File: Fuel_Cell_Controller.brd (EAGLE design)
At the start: 203.2 x 163.8 mm, 127 parts, among them J1 BLUETOOTH, U1 MAX232PTH

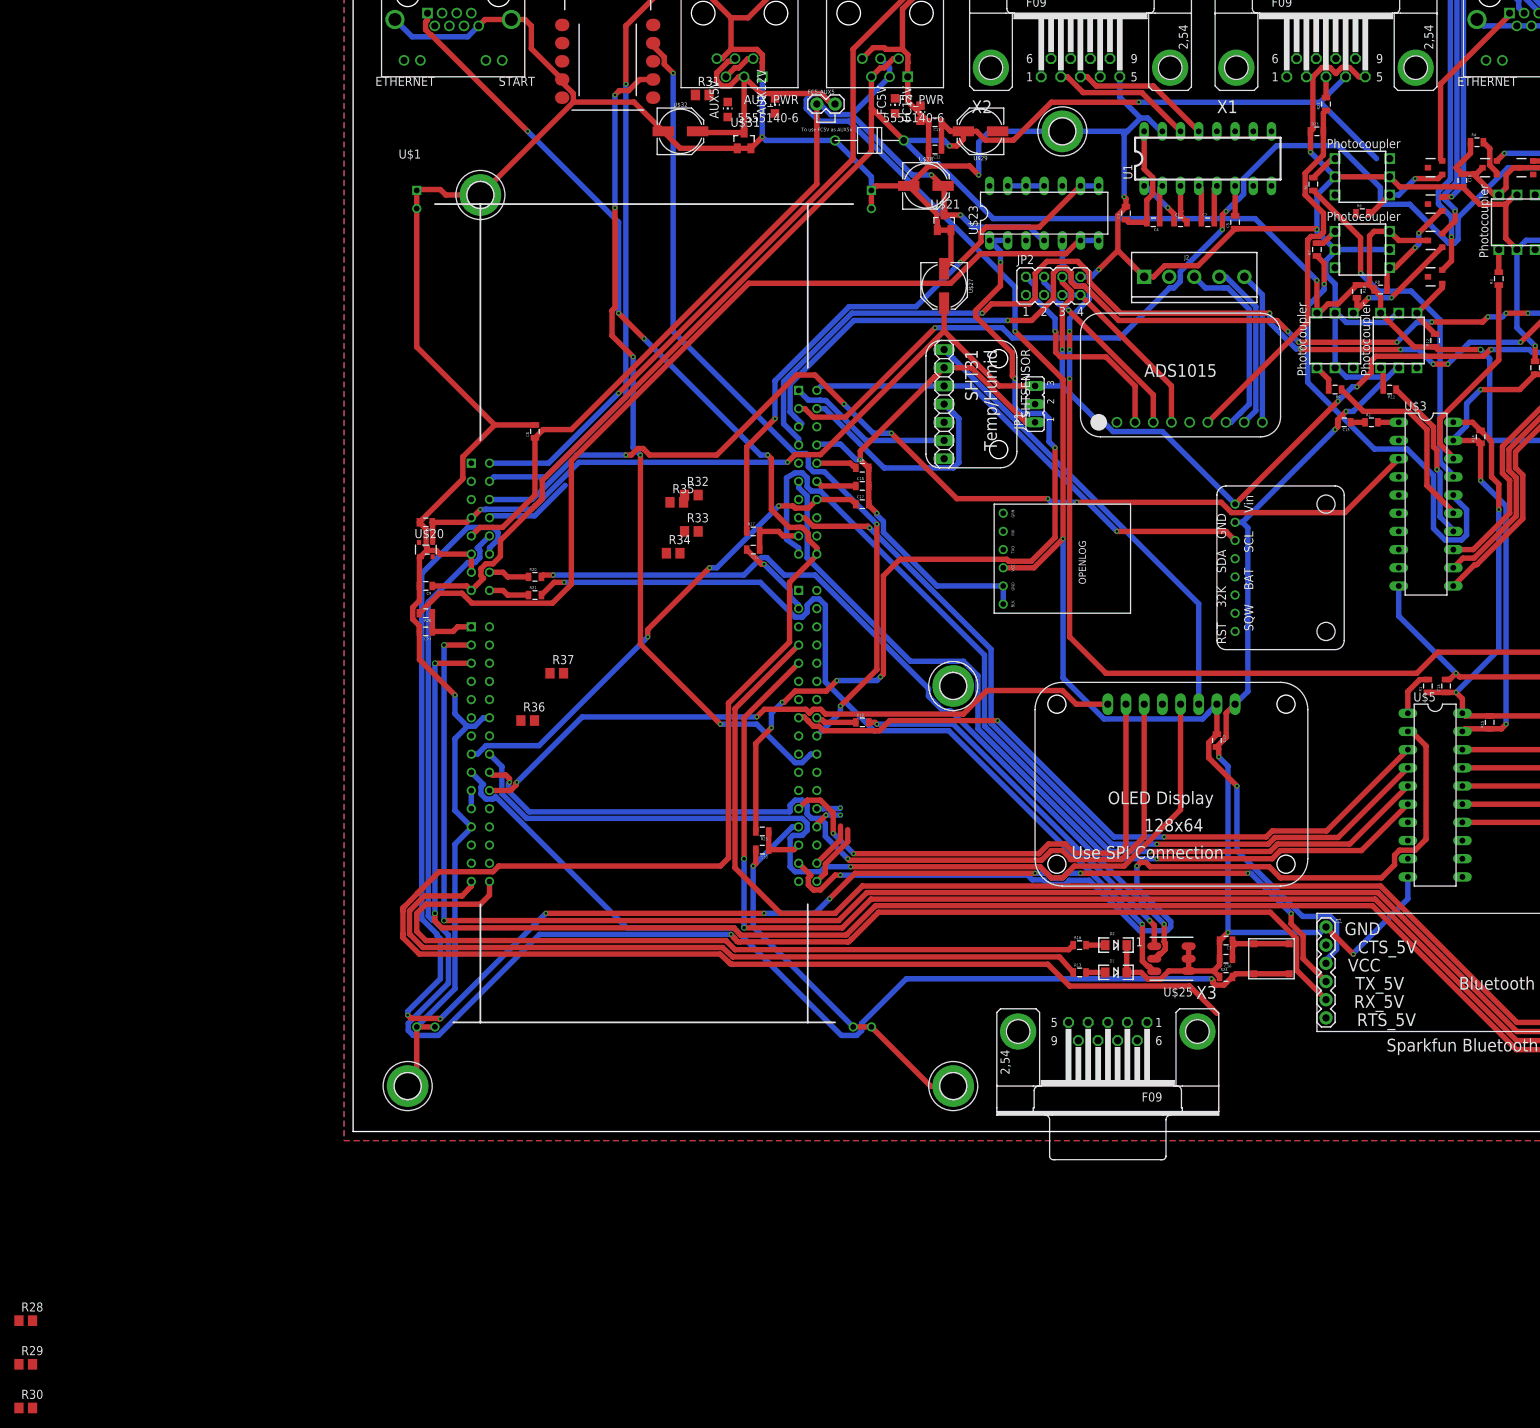
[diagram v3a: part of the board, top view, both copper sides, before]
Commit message: Added some changes in the Schematic to the Board
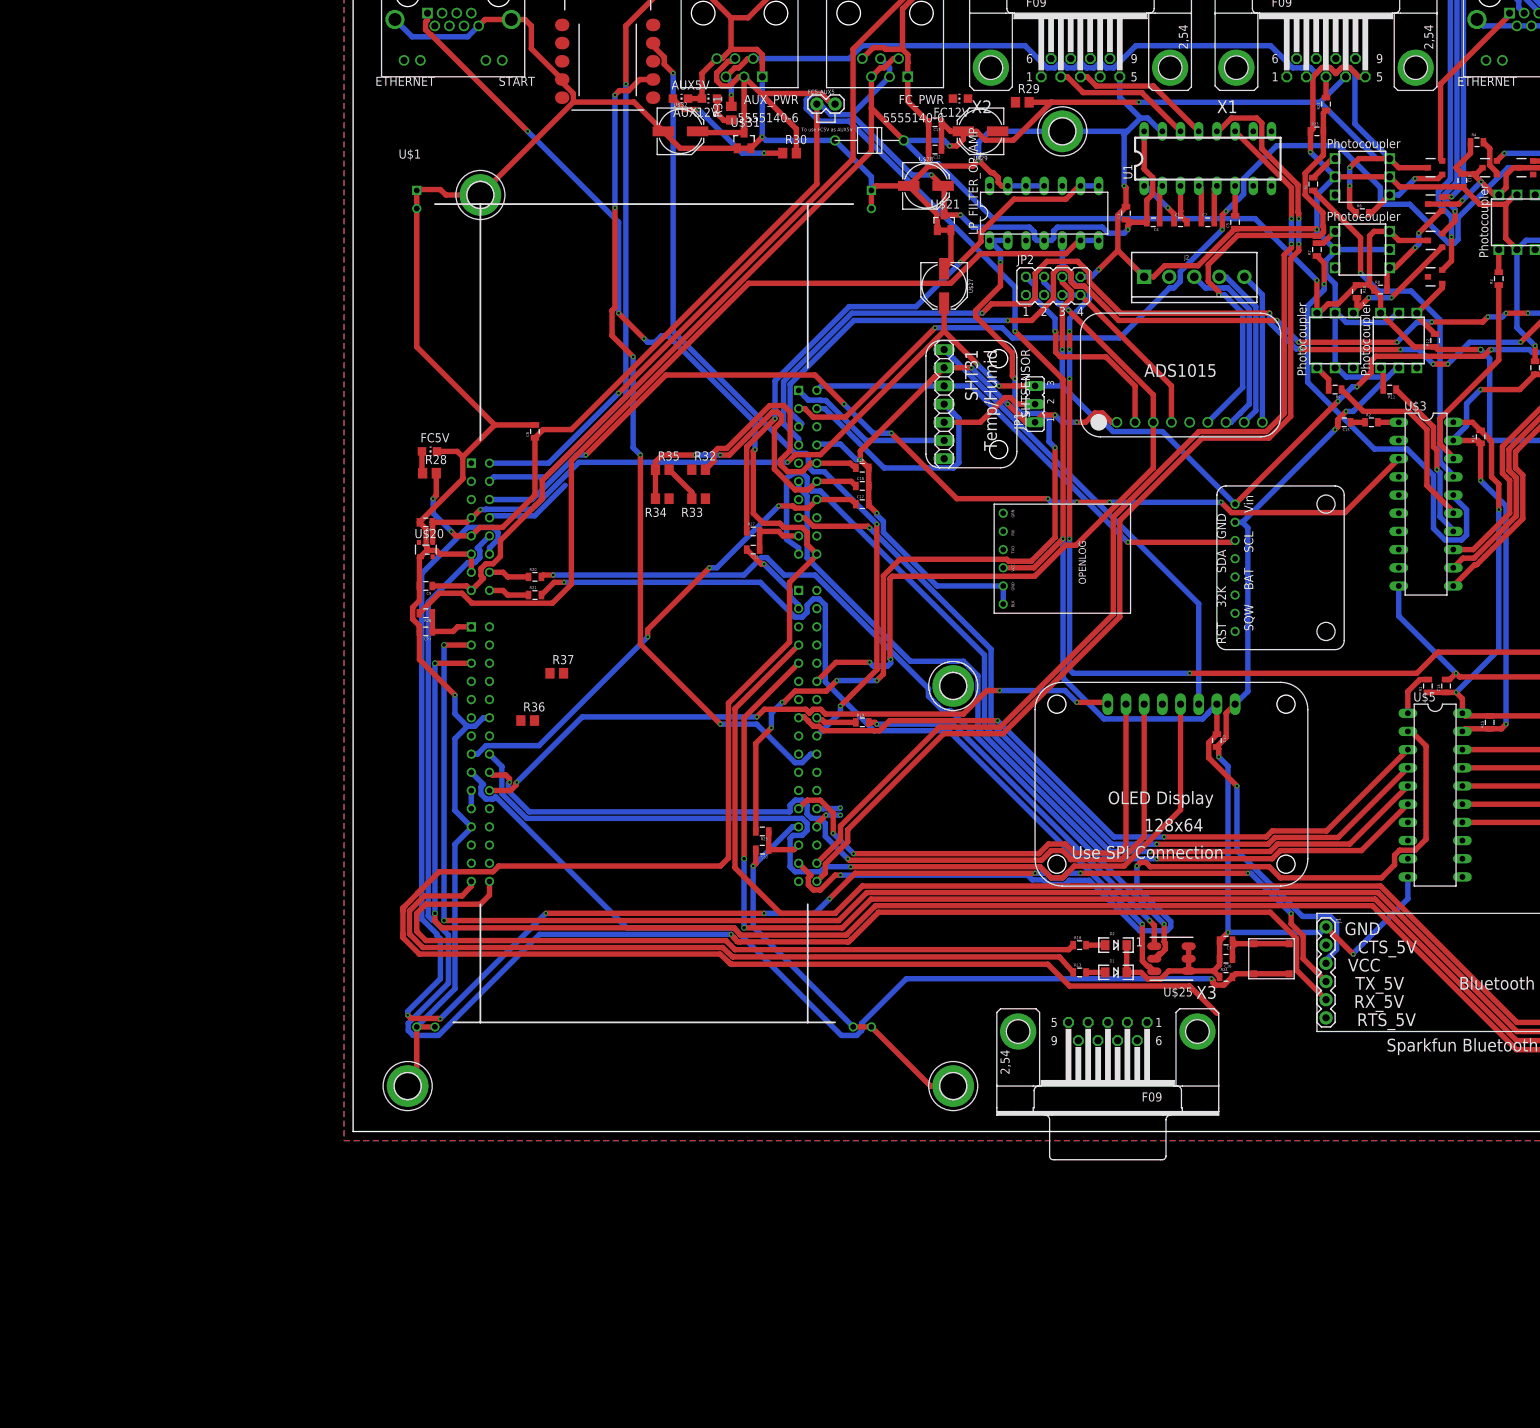
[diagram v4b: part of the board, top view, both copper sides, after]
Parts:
- moved R29 224.6 mm to (93.5, 143.8)
- moved R30 205.2 mm to (61.0, 136.7)
- moved R28 131.1 mm to (10.7, 91.9)
- moved FC5V 81.0 mm to (10.7, 95.0), turned to 270 degrees
- moved AUX12V 9.20 mm to (49.8, 144.3), turned to 90 degrees
- moved R34 7.77 mm to (43.2, 88.4), turned to 180 degrees
- moved AUX5V 6.78 mm to (45.7, 144.3), turned to 270 degrees
- moved FC12V 5.95 mm to (84.8, 144.3), turned to 90 degrees
- moved R35 5.00 mm to (43.2, 92.5)
- moved R31 4.79 mm to (52.8, 142.2), turned to 90 degrees
- moved R33 4.68 mm to (48.3, 88.4), turned to 180 degrees
- moved R32 3.70 mm to (48.3, 92.5)
- renumbered U$23 to LP_FILTER_OP_AMP
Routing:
- net MOTOR_RX: track 9.02 -> 153.6 mm, vias 0 -> 2
- net MOTOR_TX: track 6.57 -> 143.4 mm, vias 0 -> 2
- net AUX12V: track 4.86 -> 134.4 mm, vias 0 -> 3
- net I2C4_SDA: track 26.9 -> 100.1 mm, vias 1 -> 3
- net MOTOR_CURR: track 5.72 -> 47.0 mm, vias 0 -> 2
- net GND: track 1306.4 -> 1341.2 mm, vias 20 -> 24
- net FC_CURR: track 5.72 -> 36.2 mm
- net FC5V: track 265.0 -> 292.7 mm, vias 7 -> 10
- net N$25: track 0.00 -> 18.5 mm, vias 0 -> 2
- net SHT_ADR: track 0.00 -> 14.5 mm
- net FC12V: track 482.1 -> 493.9 mm, vias 5 -> 7
- net MASS_FLOW: track 53.2 -> 63.8 mm, vias 0 -> 1
- net AUX5V: track 222.5 -> 232.9 mm
- net N$28: track 0.00 -> 4.50 mm
- net _START: track 318.7 -> 322.4 mm
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
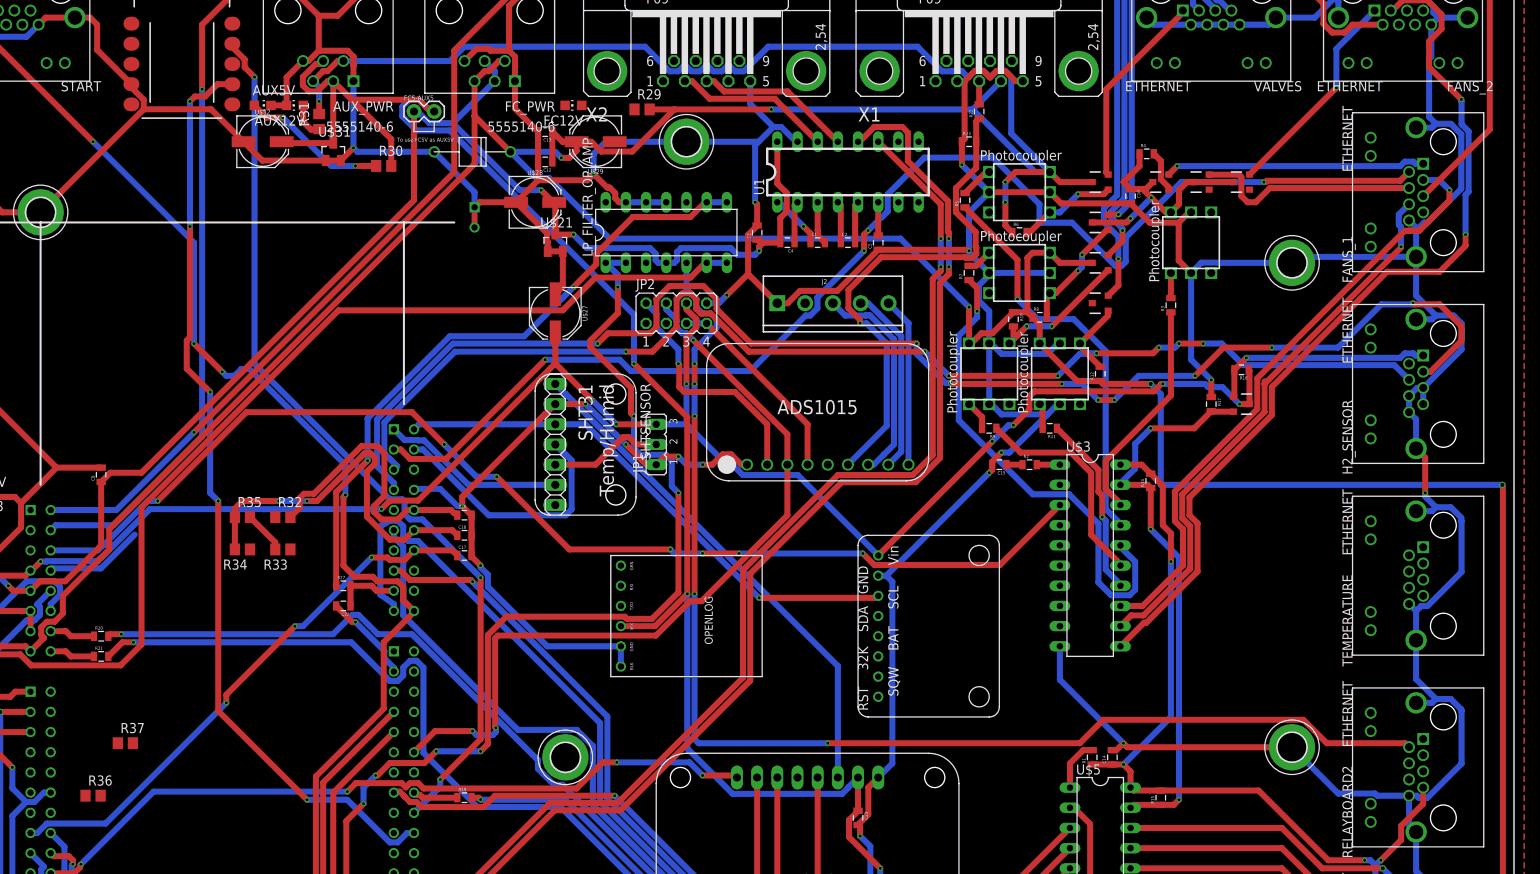
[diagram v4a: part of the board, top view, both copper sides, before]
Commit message: Continued Routing the FCC Board
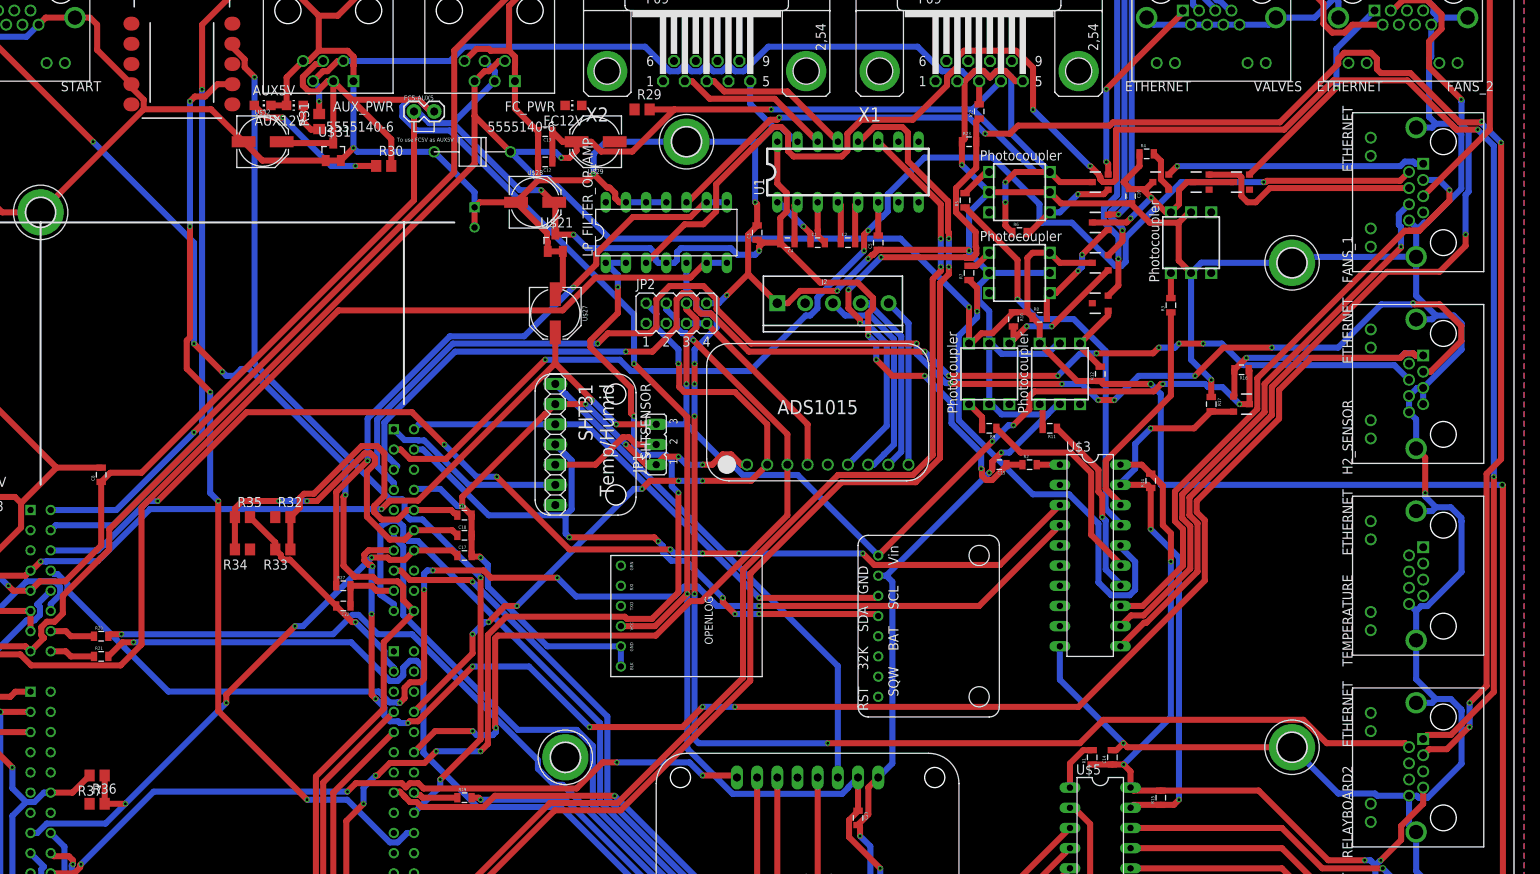
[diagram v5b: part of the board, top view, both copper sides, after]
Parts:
- moved R37 5.40 mm to (24.9, 59.9), turned to 180 degrees
- moved R36 1.14 mm to (24.9, 56.4)
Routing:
- net FC_VOLT: track 0.00 -> 229.3 mm, vias 0 -> 4
- net CAP_VOLT: track 0.00 -> 200.5 mm, vias 0 -> 6
- net STOP: track 28.1 -> 220.1 mm, vias 1 -> 9
- net _PURGE_VALVE: track 12.5 -> 156.9 mm, vias 0 -> 5
- net I2C4_SCL: track 30.4 -> 89.1 mm, vias 1 -> 7
- net FC5V: track 292.7 -> 342.4 mm, vias 10 -> 14
- net I2C1_SDA: track 32.6 -> 79.3 mm, vias 0 -> 5
- net GND: track 1341.2 -> 1358.4 mm, vias 24 -> 26
- net CAP_CURR: track 69.5 -> 75.7 mm, vias 3 -> 4
- net FC_CURR: track 36.2 -> 40.2 mm
- net SUPPLY_VALVE_ENET: vias 0 -> 2
- net MASS_FLOW: vias 1 -> 3
